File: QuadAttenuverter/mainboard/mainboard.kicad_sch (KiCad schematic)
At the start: 60 parts, among them J1 Conn_01x09, J2 Conn_02x10_Counter_Clockwise, J3 Conn_02x05_Odd_Even, U1 LM324, U2 LM324, U3 LM324, U4 LM324, U5 LM324

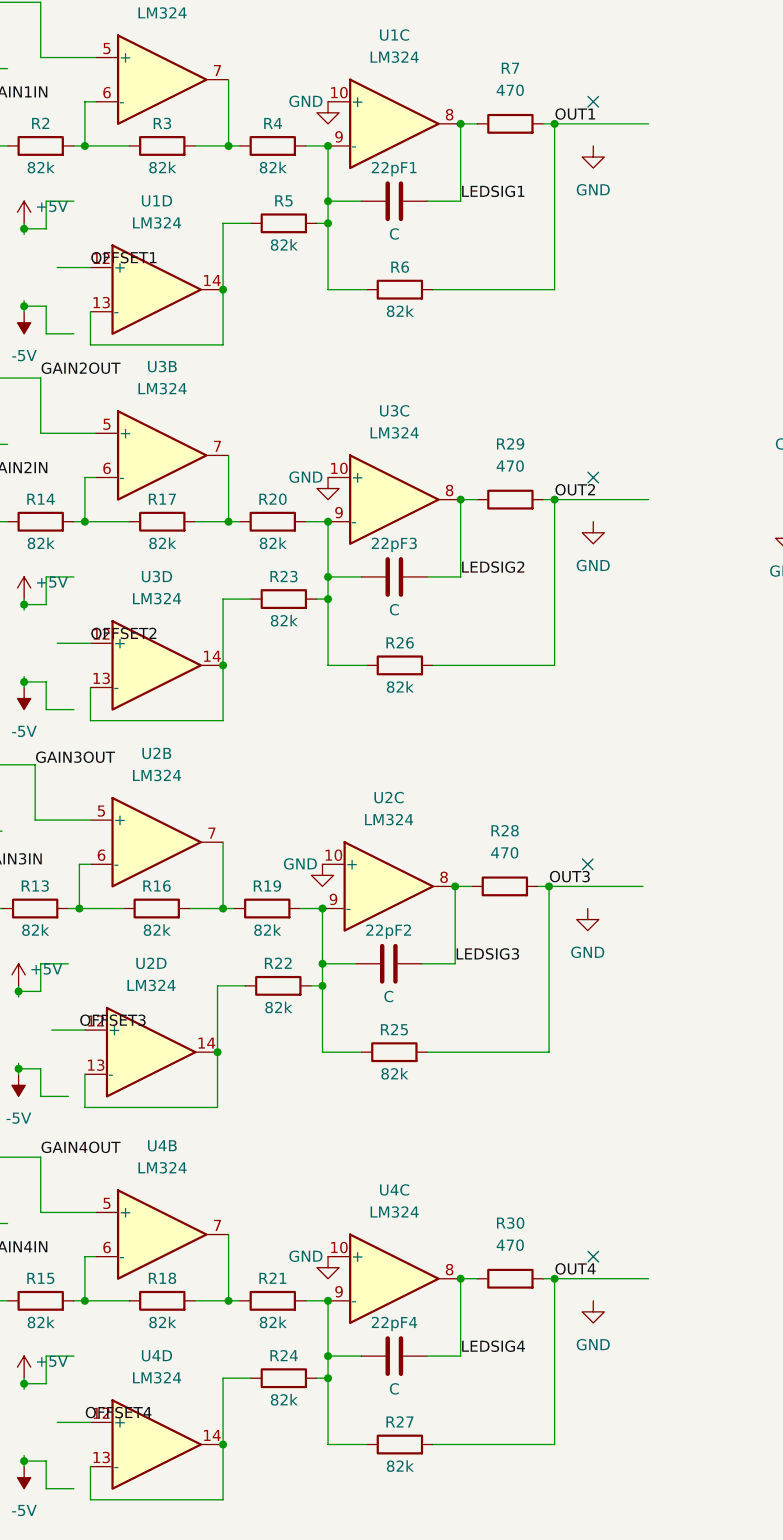
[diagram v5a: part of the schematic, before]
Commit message: Few faceplate cleanups to get rid of warnings
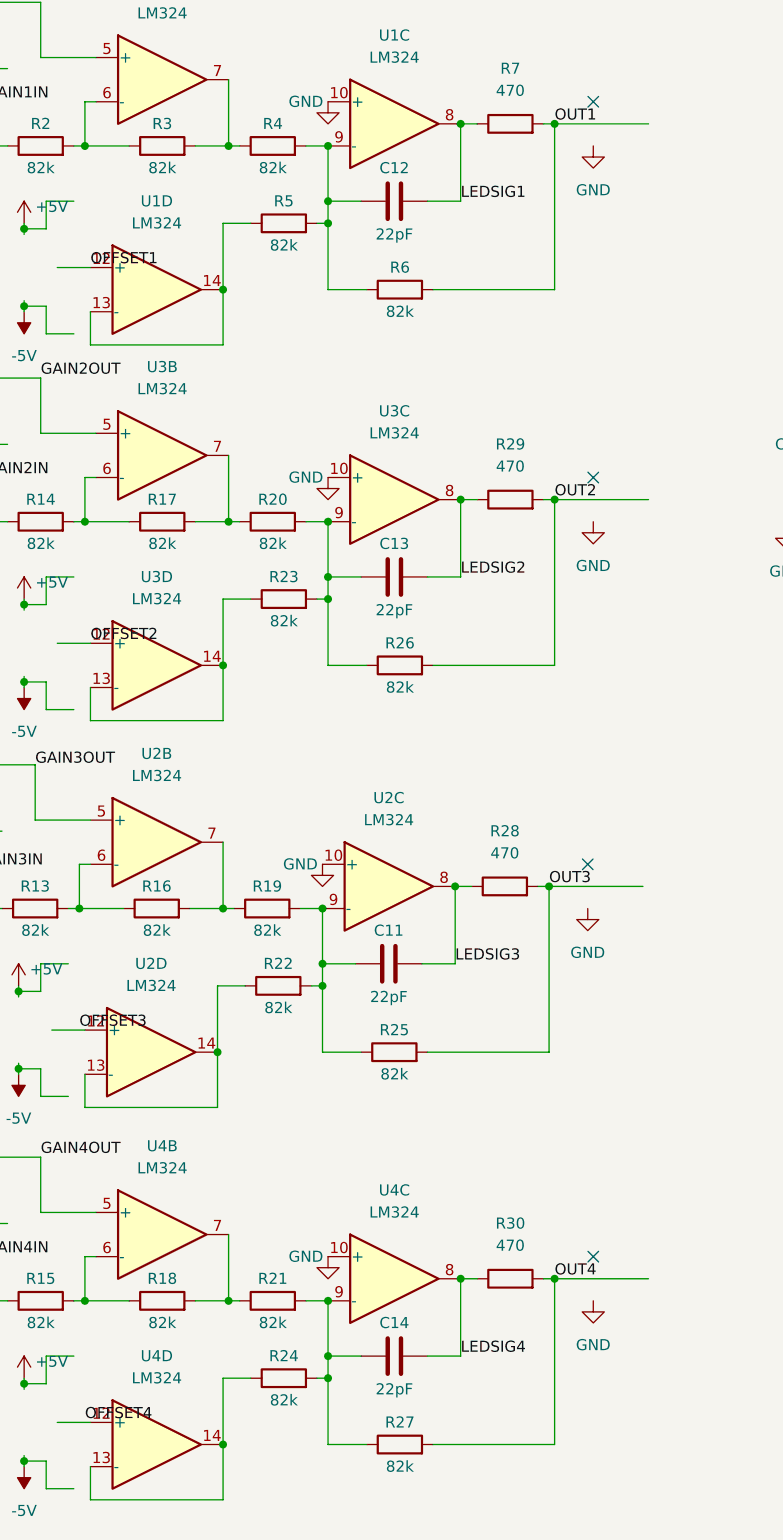
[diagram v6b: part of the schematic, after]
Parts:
- C11: renamed from 22pF2; value C -> 22pF
- C12: renamed from 22pF1; value C -> 22pF
- C13: renamed from 22pF3; value C -> 22pF
- C14: renamed from 22pF4; value C -> 22pF
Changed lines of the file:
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@@
   (symbol (lib_id "Device:C") (at 122.555 170.815 90) (unit 1)
     (in_bom yes) (on_board yes)
-    (property "Reference" "22pF4" (id 0) (at 122.555 167.005 90))
-    (property "Value" "C" (id 1) (at 122.555 174.625 90))
+    (property "Reference" "C14" (id 0) (at 122.555 167.005 90))
+    (property "Value" "22pF" (id 1) (at 122.555 174.625 90))
     (property "Footprint" "Capacitor_SMD:C_0603_1608Metric_Pad1.08x0.95mm_HandSolder" (id 2) (at 126.365 169.8498 0)
       (effects (font (size 1.27 1.27)) hide)
@@
   (symbol (lib_id "Device:C") (at 121.92 125.73 90) (unit 1)
     (in_bom yes) (on_board yes)
-    (property "Reference" "22pF2" (id 0) (at 121.92 121.92 90))
-    (property "Value" "C" (id 1) (at 121.92 129.54 90))
+    (property "Reference" "C11" (id 0) (at 121.92 121.92 90))
+    (property "Value" "22pF" (id 1) (at 121.92 129.54 90))
     (property "Footprint" "Capacitor_SMD:C_0603_1608Metric_Pad1.08x0.95mm_HandSolder" (id 2) (at 125.73 124.7648 0)
       (effects (font (size 1.27 1.27)) hide)
@@
   (symbol (lib_id "Device:C") (at 122.555 38.1 90) (unit 1)
     (in_bom yes) (on_board yes)
-    (property "Reference" "22pF1" (id 0) (at 122.555 34.29 90))
-    (property "Value" "C" (id 1) (at 122.555 41.91 90))
+    (property "Reference" "C12" (id 0) (at 122.555 34.29 90))
+    (property "Value" "22pF" (id 1) (at 122.555 41.91 90))
     (property "Footprint" "Capacitor_SMD:C_0603_1608Metric_Pad1.08x0.95mm_HandSolder" (id 2) (at 126.365 37.1348 0)
       (effects (font (size 1.27 1.27)) hide)
@@
   (symbol (lib_id "Device:C") (at 122.555 81.28 90) (unit 1)
     (in_bom yes) (on_board yes)
-    (property "Reference" "22pF3" (id 0) (at 122.555 77.47 90))
-    (property "Value" "C" (id 1) (at 122.555 85.09 90))
+    (property "Reference" "C13" (id 0) (at 122.555 77.47 90))
+    (property "Value" "22pF" (id 1) (at 122.555 85.09 90))
     (property "Footprint" "Capacitor_SMD:C_0603_1608Metric_Pad1.08x0.95mm_HandSolder" (id 2) (at 126.365 80.3148 0)
       (effects (font (size 1.27 1.27)) hide)
@@
       (reference "#PWR0155") (unit 1) (value "GND") (footprint "")
     )
-    (path "/cf08a499-63ac-4d34-9db9-13bdec934fb1"
-      (reference "22pF1") (unit 1) (value "C") (footprint "Capacitor_SMD:C_0603_1608Metric_Pad1.08x0.95mm_HandSolder")
-    )
-    (path "/619b4a24-dbe5-4d77-a0e4-9efc2cdbe4a1"
-      (reference "22pF2") (unit 1) (value "C") (footprint "Capacitor_SMD:C_0603_1608Metric_Pad1.08x0.95mm_HandSolder")
-    )
-    (path "/f6bf49e3-46e7-4f79-9c27-b1bd1311d85a"
-      (reference "22pF3") (unit 1) (value "C") (footprint "Capacitor_SMD:C_0603_1608Metric_Pad1.08x0.95mm_HandSolder")
-    )
-    (path "/1e10f547-542d-4e39-bb1f-868ef88ad8bd"
-      (reference "22pF4") (unit 1) (value "C") (footprint "Capacitor_SMD:C_0603_1608Metric_Pad1.08x0.95mm_HandSolder")
-    )
     (path "/2744eae7-e0bd-481e-b42c-af00034b2d86"
       (reference "C1") (unit 1) (value "100n") (footprint "Capacitor_SMD:C_0603_1608Metric_Pad1.08x0.95mm_HandSolder")
@@
       (reference "C10") (unit 1) (value "100n") (footprint "Capacitor_SMD:C_0603_1608Metric_Pad1.08x0.95mm_HandSolder")
     )
+    (path "/619b4a24-dbe5-4d77-a0e4-9efc2cdbe4a1"
+      (reference "C11") (unit 1) (value "22pF") (footprint "Capacitor_SMD:C_0603_1608Metric_Pad1.08x0.95mm_HandSolder")
+    )
+    (path "/cf08a499-63ac-4d34-9db9-13bdec934fb1"
+      (reference "C12") (unit 1) (value "22pF") (footprint "Capacitor_SMD:C_0603_1608Metric_Pad1.08x0.95mm_HandSolder")
+    )
+    (path "/f6bf49e3-46e7-4f79-9c27-b1bd1311d85a"
+      (reference "C13") (unit 1) (value "22pF") (footprint "Capacitor_SMD:C_0603_1608Metric_Pad1.08x0.95mm_HandSolder")
+    )
+    (path "/1e10f547-542d-4e39-bb1f-868ef88ad8bd"
+      (reference "C14") (unit 1) (value "22pF") (footprint "Capacitor_SMD:C_0603_1608Metric_Pad1.08x0.95mm_HandSolder")
+    )
     (path "/bb61042d-c611-4ef3-baea-41d687cdc4ff"

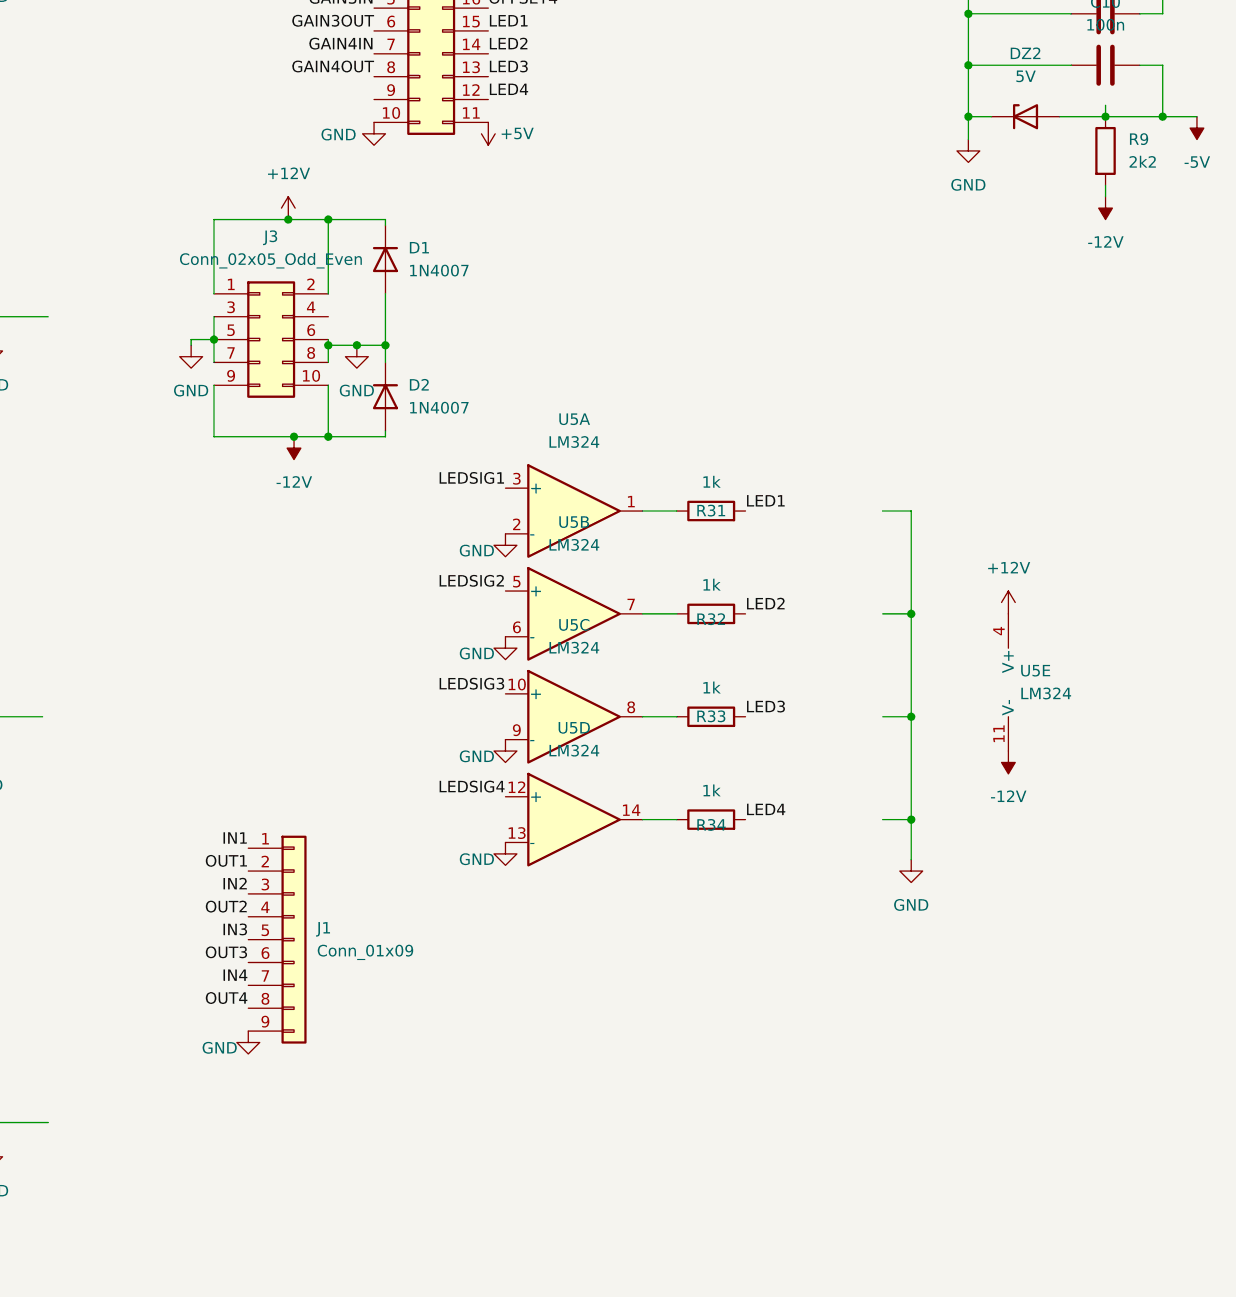
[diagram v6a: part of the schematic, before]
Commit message: Add electrolytic caps and inrush resistors
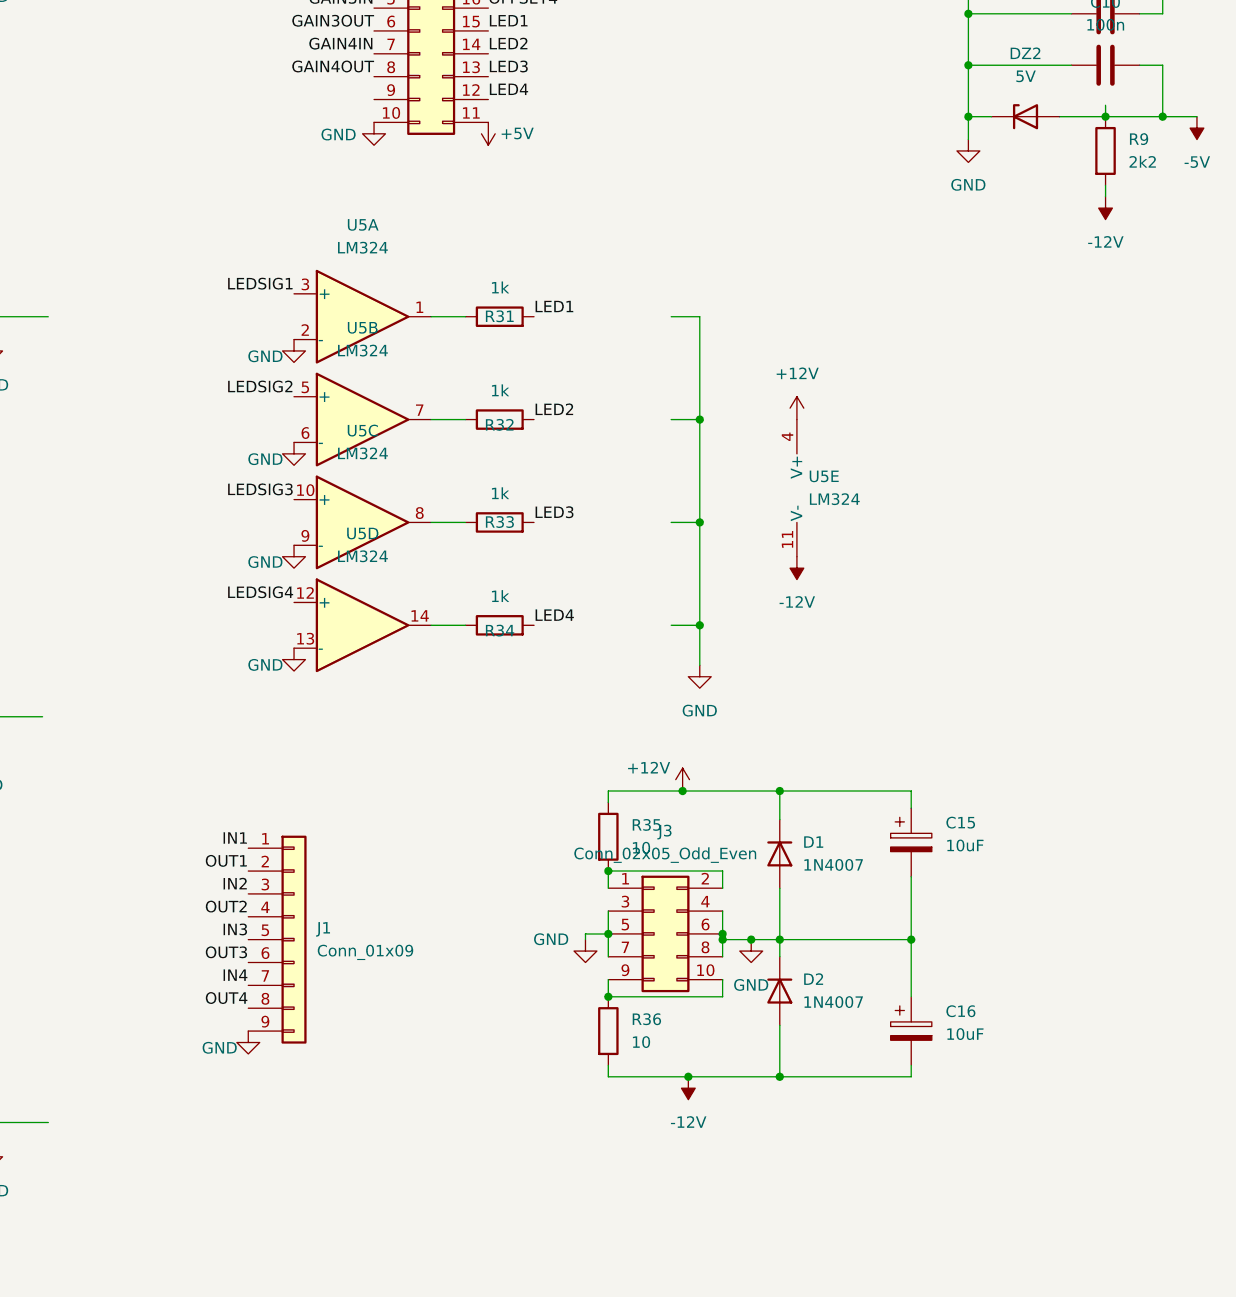
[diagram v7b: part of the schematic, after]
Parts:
- added C15, C16: 10uF, Capacitor_THT:CP_Radial_D5.0mm_P2.00mm, symbol Device:C_Polarized
- added R35, R36: 10, Resistor_SMD:R_0603_1608Metric_Pad0.98x0.95mm_HandSolder, symbol Device:R
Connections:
- net +12V: now also C15.1, R35.1; no longer J3.1 (Pin_1), J3.2 (Pin_2)
- net -12V: now also C16.2, R36.2; no longer J3.10 (Pin_10), J3.9 (Pin_9)
- net GND: now also J3.4 (Pin_4), C15.2, C16.1
- new net: J3.10 (Pin_10), J3.9 (Pin_9), R36.1
- new net: J3.1 (Pin_1), J3.2 (Pin_2), R35.2
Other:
- moved on the sheet: D1, D2, J3, R31, R32, R33, R34, U5A, U5B, U5C, U5D, U5E

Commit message: Adjusted LM324 to actual SO14 package
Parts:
- U1, U2, U3, U4, U5: footprint Package_SO:SO-14_5.3x10.2mm_P1.27mm -> Package_SO:SO-14_3.9x8.65mm_P1.27mm
